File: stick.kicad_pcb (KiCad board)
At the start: 2 copper layers, 87.6 x 48.3 mm, 18 parts, among them P1 RF7021SE, P4 HOST_SER, U1 stm32f103c8t6-module-china

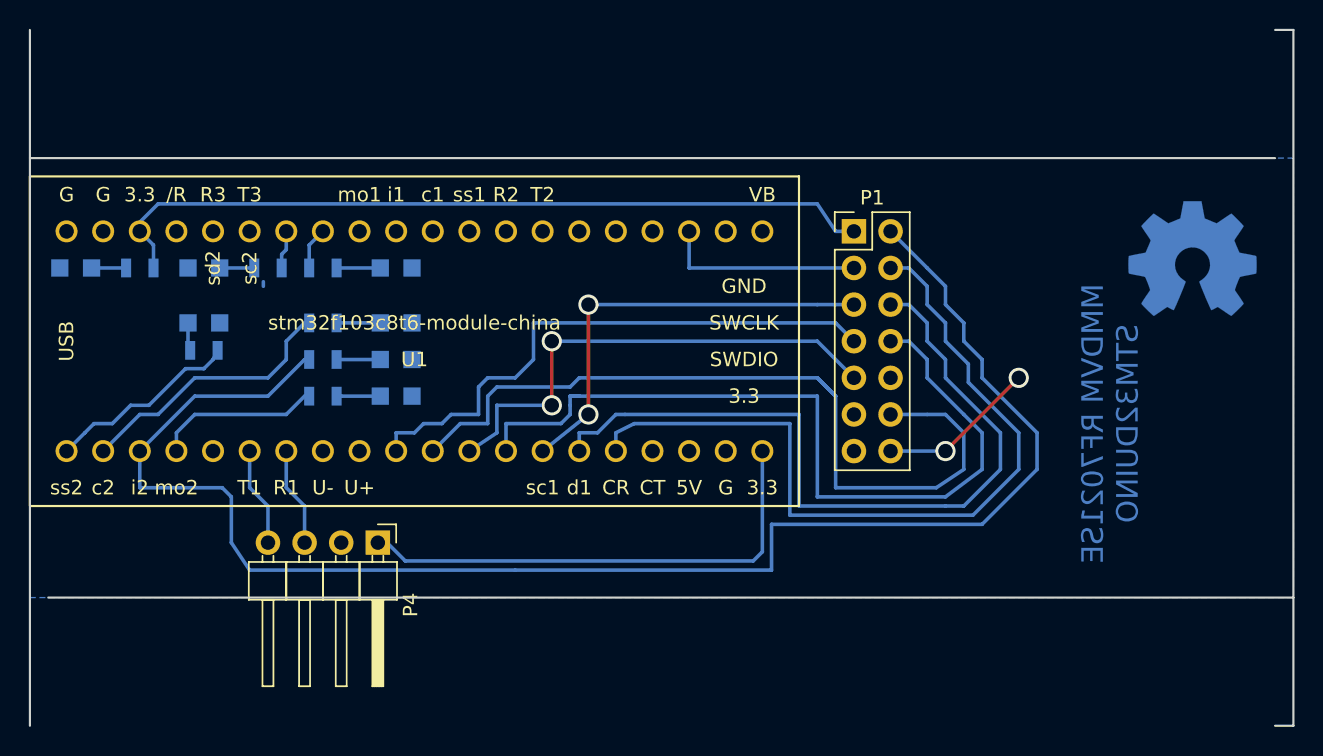
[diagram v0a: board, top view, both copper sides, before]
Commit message: Changed case to hold RPI Zero internally. Case may be a little to wide for machined boards, in this case adjust pcb_l after test print of some millimeters of height.
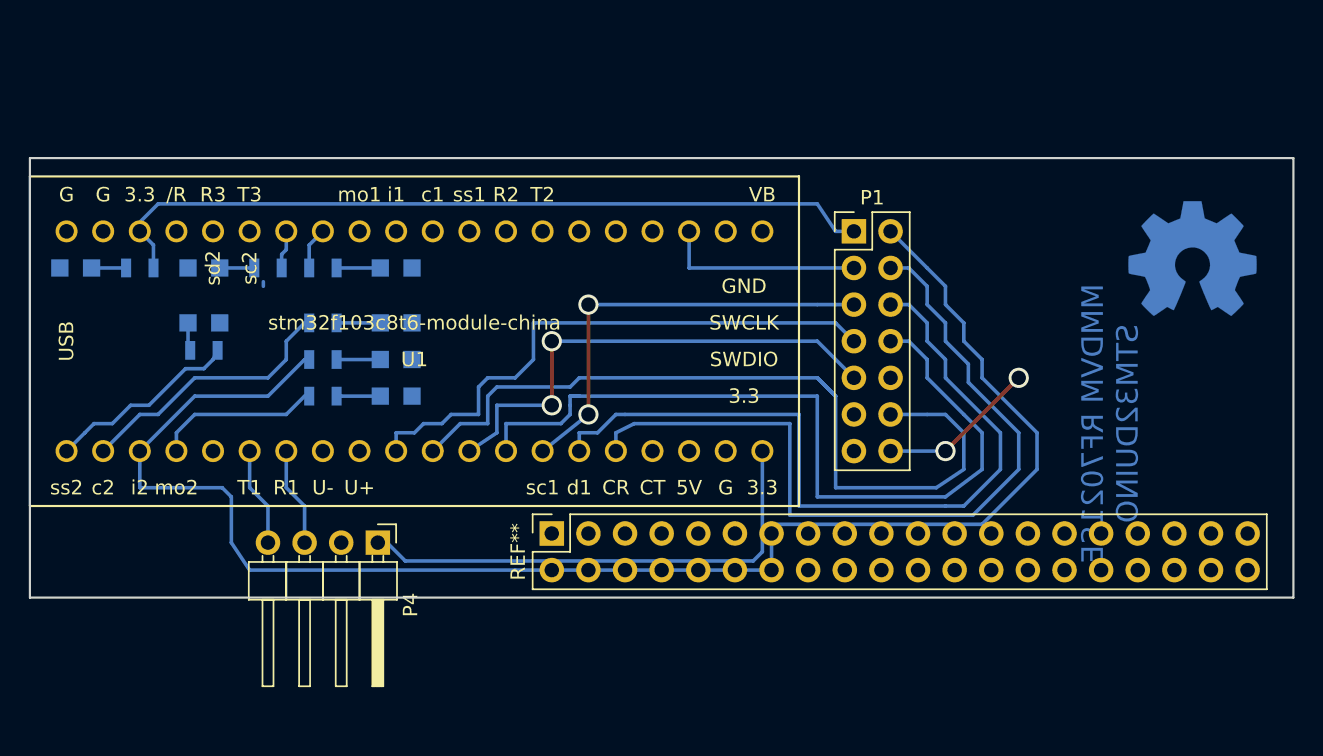
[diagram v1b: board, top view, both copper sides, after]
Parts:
- added REF**: Socket_Strip_Straight_2x20_Pitch2.54mm, Socket_Strips:Socket_Strip_Straight_2x20_Pitch2.54mm, F.Cu at (136.5, 70.5)
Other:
- board size 87.6 x 48.3 mm -> 87.6 x 30.5 mm

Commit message: Added smaller footprint board which is NOT singlesided if you want the serial display or I2C display However,  very few simple wires will do the job if you don't have the ability to do a two sided PCB.
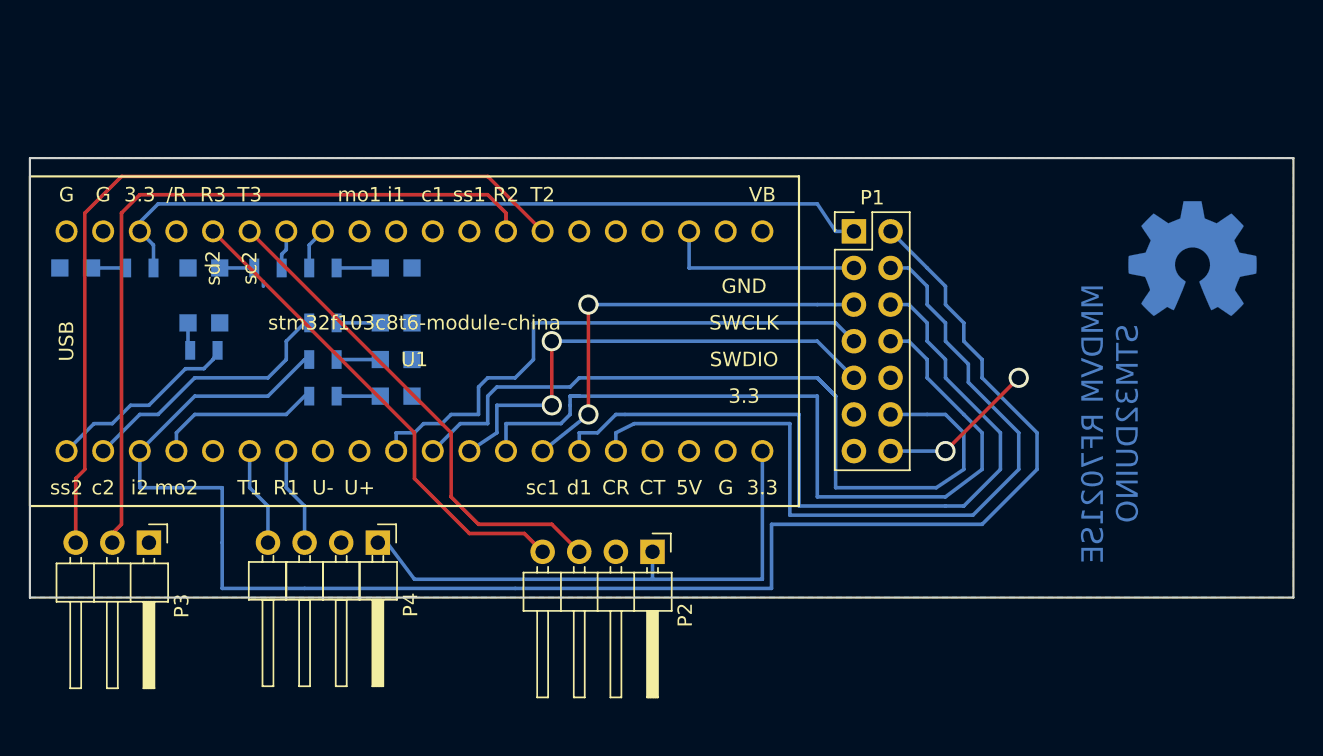
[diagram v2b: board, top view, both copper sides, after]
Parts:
- removed REF**: Socket_Strip_Straight_2x20_Pitch2.54mm, Socket_Strips:Socket_Strip_Straight_2x20_Pitch2.54mm
- added P2: DISP_I2C, Pin_Headers:Pin_Header_Angled_1x04_Pitch2.54mm, F.Cu at (143.5, 71.8)
- added P3: DISP_SER, Pin_Headers:Pin_Header_Angled_1x03_Pitch2.54mm, F.Cu at (108.6, 71.1)
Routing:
- net DISP_TX: track 0.00 -> 57.5 mm
- net DISP_RX: track 0.00 -> 52.1 mm
- net Net-(P2-Pad3): track 0.00 -> 34.7 mm
- net Net-(P2-Pad4): track 0.00 -> 33.9 mm
- net +3V3: track 89.5 -> 93.8 mm
- net PAC: track 109.1 -> 112.9 mm
- added copper zone on F.Cu, net GND

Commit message: Finalized new "stick" design. Added gerbers.
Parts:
- added REF**: , Pin_Headers:Pin_Header_Straight_1x01_Pitch1.00mm, F.Cu at (130.6, 57.4)
- moved D7 20.1 mm to (123.4, 54.4)
- moved R7 19.7 mm to (127.5, 54.4)
- moved D1 16.2 mm to (110.7, 62.0)
- moved D6 15.7 mm to (110.7, 56.9), turned to 0 degrees
- moved R1 15.7 mm to (106.2, 62.0)
- moved REF*** 11.9 mm to (169.2, 50.3)
- moved R6 7.19 mm to (115.3, 56.9), turned to 180 degrees
- moved R3 6.44 mm to (106.2, 59.4), turned to 0 degrees
- moved R4 5.99 mm to (115.8, 62.0)
- moved R5 5.06 mm to (115.8, 59.4)
- moved D4 4.23 mm to (123.4, 62.0)
- moved D3 3.92 mm to (110.7, 59.4)
- moved D2 2.82 mm to (110.7, 54.4)
- moved D5 2.75 mm to (123.4, 59.4)
- moved R2 2.75 mm to (115.3, 54.4)
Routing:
- net Net-(P2-Pad3): track 34.7 -> 50.7 mm, vias 0 -> 2
- net LEDDMR: track 18.7 -> 2.87 mm
- net Net-(P2-Pad4): track 33.9 -> 45.6 mm, vias 0 -> 2
- net PAC: track 112.9 -> 104.3 mm
- net DISP_TX: track 57.5 -> 65.5 mm, vias 0 -> 2
- net LEDDSTAR: track 13.5 -> 7.24 mm
- net LEDP25: track 2.93 -> 9.18 mm
- net +3V3: track 93.8 -> 97.7 mm
- net LED_COS: track 11.5 -> 7.75 mm
- net DISP_RX: track 52.1 -> 48.6 mm, vias 0 -> 2
- net Net-(D5-Pad2): track 3.03 -> 5.57 mm
- net Net-(D4-Pad2): track 3.03 -> 5.57 mm
- net LEDYSF: track 3.76 -> 5.94 mm
- net Net-(D3-Pad2): track 1.97 -> 2.52 mm
- net Net-(D6-Pad2): track 3.03 -> 2.52 mm
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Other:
- board text added: "MMDVM Hotspot RF7021SE+STM32DUINO © DB4PLE License: CC-BY-SA 3.0"
- board text removed: "MMDVM RF7021SE STM32DUINO"
